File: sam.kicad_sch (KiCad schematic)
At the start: 46 parts, among them IC1 4164, IC10 74ACT138, IC15 MC6883, IC16 74LS244N, IC2 4164, IC3 4164, IC31 74LS02N, IC33 74ACT138N, IC36 74LS132, IC37 GAL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

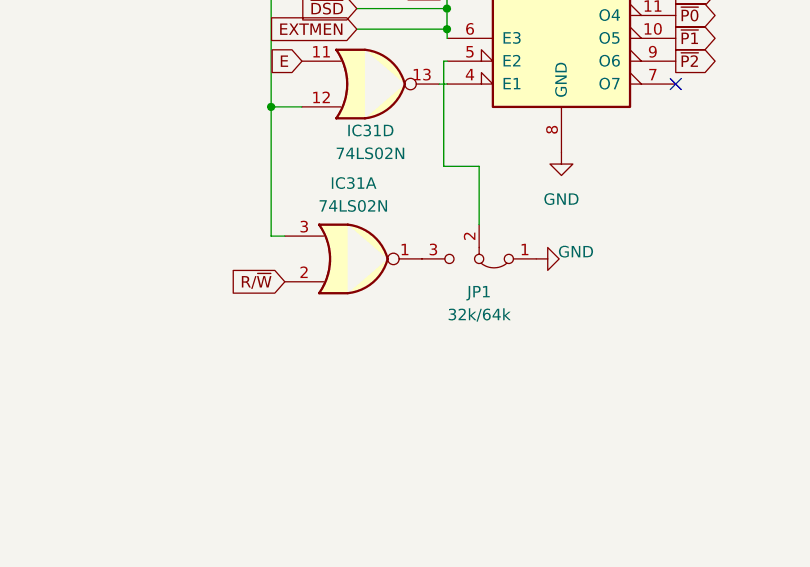
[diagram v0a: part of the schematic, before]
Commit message: rework keyboard type selection
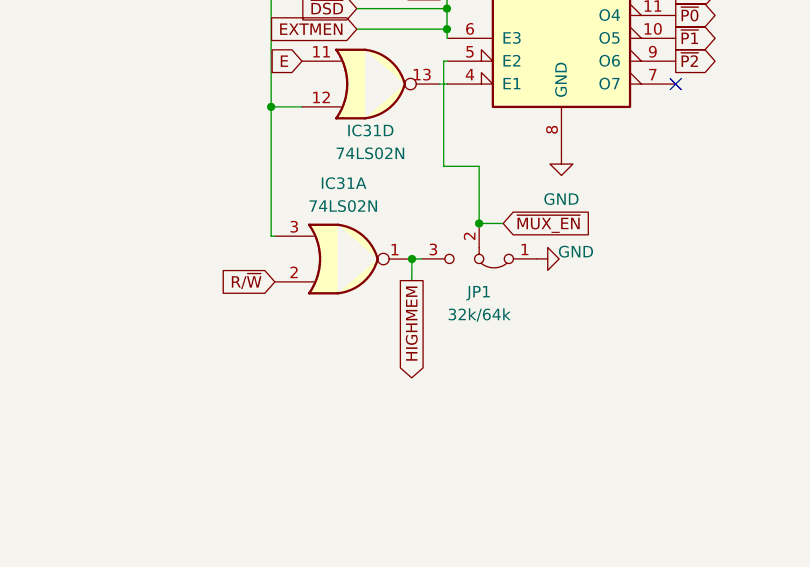
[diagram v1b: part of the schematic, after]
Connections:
- net ~{MUX_EN}: now reaches IC33.5 (E2), JP1.2 (C)
- net HIGHMEM: now reaches IC31.1, JP1.3 (B)
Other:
- moved on the sheet: IC31A
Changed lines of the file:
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@@
 	)
 	(junction
+		(at 112.903 191.77)
+		(diameter 0)
+		(color 0 0 0 0)
+	)
+	(junction
 		(at 89.789 163.576)
 		(diameter 0)
@@
 	)
 	(junction
+		(at 105.4417 195.7201)
+		(diameter 0)
+		(color 0 0 0 0)
+	)
+	(junction
 		(at 66.929 85.344)
 		(diameter 0)
@@
 	(wire
 		(pts
-			(xy 89.789 193.167) (xy 91.313 193.167)
+			(xy 89.789 193.167) (xy 90.2017 193.1801)
 		)
 		(stroke
@@
 	(wire
 		(pts
+			(xy 105.4417 195.7201) (xy 106.553 195.707)
+		)
+		(stroke
+			(width 0)
+			(type default)
+		)
+	)
+	(wire
+		(pts
 			(xy 244.856 24.003) (xy 244.856 24.384)
 		)
@@
 	(wire
 		(pts
-			(xy 112.903 185.42) (xy 112.903 191.897)
+			(xy 112.903 185.42) (xy 112.903 191.77)
 		)
 		(stroke
@@
 	(wire
 		(pts
+			(xy 115.57 191.77) (xy 112.903 191.77)
+		)
+		(stroke
+			(width 0)
+			(type default)
+		)
+	)
+	(wire
+		(pts
 			(xy 24.257 85.344) (xy 25.273 85.344)
 		)
@@
 	(wire
 		(pts
+			(xy 105.41 198.12) (xy 105.4417 195.7201)
+		)
+		(stroke
+			(width 0)
+			(type default)
+		)
+	)
+	(wire
+		(pts
 			(xy 221.742 75.311) (xy 232.156 75.311)
 		)
@@
 	(wire
 		(pts
+			(xy 112.903 191.77) (xy 112.903 191.897)
+		)
+		(stroke
+			(width 0)
+			(type default)
+		)
+	)
+	(wire
+		(pts
 			(xy 24.257 21.717) (xy 24.257 24.638)
 		)
@@
 	(global_label "R{slash}~{W}"
 		(shape input)
-		(at 91.313 198.247 180)
+		(at 90.2017 198.2601 180)
 		(fields_autoplaced yes)
 		(effects
@@
 		)
 		(property "Intersheetrefs" "${INTERSHEET_REFS}"
-			(at 85.0095 198.247 0)
+			(at 83.8982 198.2601 0)
 			(effects
 				(font
@@
 		)
 	)
+	(global_label "~{MUX_EN}"
+		(shape input)
+		(at 115.57 191.77 0)
+		(fields_autoplaced yes)
+		(effects
+			(font
+				(size 1.27 1.27)
+			)
+			(justify left)
+		)
+		(property "Intersheetrefs" "${INTERSHEET_REFS}"
+			(at 125.3395 191.77 0)
+			(effects
+				(font
+					(size 1.27 1.27)
+				)
+				(justify left)
+				(hide yes)
+			)
+		)
+	)
 	(global_label "~{DSD}"
 		(shape output)
@@
 		)
 	)
+	(global_label "HIGHMEM"
+		(shape output)
+		(at 105.41 198.12 270)
+		(fields_autoplaced yes)
+		(effects
+			(font
+				(size 1.27 1.27)
+			)
+			(justify right)
+		)
+		(property "Intersheetrefs" "${INTERSHEET_REFS}"
+			(at 105.41 209.0386 90)
+			(effects
+				(font
+					(size 1.27 1.27)
+				)
+				(justify right)
+				(hide yes)
+			)
+		)
+	)
 	(global_label "Z5"
 		(shape input)
@@
 	(symbol
 		(lib_id "74xx:74LS02")
-		(at 98.933 195.707 0)
+		(at 97.8217 195.7201 0)
 		(mirror x)
 		(unit 1)
@@
 		(fields_autoplaced yes)
 		(property "Reference" "IC31"
-			(at 98.933 187.325 0)
+			(at 97.8217 187.3381 0)
 			(effects
 				(font
@@
 		)
 		(property "Value" "74LS02N"
-			(at 98.933 189.865 0)
+			(at 97.8217 189.8781 0)
 			(effects
 				(font
@@
 		)
 		(property "Footprint" "Package_DIP:DIP-14_W7.62mm"
-			(at 98.933 195.707 0)
+			(at 97.8217 195.7201 0)
 			(effects
 				(font
@@
 		)
 		(property "Datasheet" "http://www.ti.com/lit/gpn/sn74ls02"
-			(at 98.933 195.707 0)
+			(at 97.8217 195.7201 0)
 			(effects
 				(font
@@
 		)
 		(property "Description" ""
-			(at 98.933 195.707 0)
+			(at 97.8217 195.7201 0)
 			(effects
 				(font
@@
 		)
 		(property "DigiKey" "296-1627-5-ND"
-			(at 98.933 195.707 0)
+			(at 97.8217 195.7201 0)
 			(effects
 				(font
@@
 		)
 		(property "SA2120" "Sheet 1 (spare)"
-			(at 98.933 195.707 0)
+			(at 97.8217 195.7201 0)
 			(effects
 				(font

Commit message: refresh BOM
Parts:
- C10, C12: value 100n -> 100nF; LCSC (none) -> C1711
- C40: LCSC (none) -> C1653
- C41: LCSC (none) -> C1663
- IC1, IC15, IC2, IC3, IC33, IC4, IC5, IC6, IC7, IC8: SA2120 Sheet 1 -> (none)
- IC10: LCSC (none) -> C1547282
- IC16: LCSC (none) -> C22374098; SA2120 Sheet 1 -> (none)
- IC31: LCSC (none) -> C22374091; SA2120 Sheet 1 (spare) -> (none)
- R12: DigiKey CF14JT22R0CT-ND -> (none); LCSC (none) -> C17561
- R19, R20, R21, R22, R23, R24, R25, R26, R27, R28, R66: LCSC (none) -> C17561
- R37: LCSC (none) -> C22843
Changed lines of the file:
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@@
 			)
 		)
-		(property "SA2120" "Sheet 1"
-			(at 35.433 42.418 0)
-			(effects
-				(font
-					(size 1.27 1.27)
-				)
-				(hide yes)
-			)
-		)
 		(pin "1"
 		)
@@
 			)
 		)
-		(property "Value" "100n"
+		(property "Value" "100nF"
 			(at 240.157 155.829 0)
 			(effects
@@
 			)
 		)
+		(property "LCSC" "C1711"
+			(at 237.236 154.686 0)
+			(effects
+				(font
+					(size 1.27 1.27)
+				)
+				(hide yes)
+			)
+		)
 		(pin "1"
 		)
@@
 			)
 		)
+		(property "LCSC" "C1547282"
+			(at 38.1 229.87 0)
+			(effects
+				(font
+					(size 1.27 1.27)
+				)
+				(hide yes)
+			)
+		)
 		(pin "1"
 		)
@@
 			)
 		)
-		(property "SA2120" "Sheet 1"
-			(at 120.777 42.545 0)
-			(effects
-				(font
-					(size 1.27 1.27)
-				)
-				(hide yes)
-			)
-		)
 		(pin "1"
 		)
@@
 			)
 		)
-		(property "SA2120" "Sheet 1"
+		(property "LCSC" "C22374098"
 			(at 35.306 168.91 0)
 			(effects
@@
 			)
 		)
+		(property "LCSC" "C17561"
+			(at 260.096 42.291 90)
+			(effects
+				(font
+					(size 1.27 1.27)
+				)
+				(hide yes)
+			)
+		)
 		(pin "1"
 		)
@@
 			)
 		)
+		(property "LCSC" "C17561"
+			(at 260.096 54.991 90)
+			(effects
+				(font
+					(size 1.27 1.27)
+				)
+				(hide yes)
+			)
+		)
 		(pin "1"
 		)
@@
 			)
 		)
+		(property "LCSC" "C17561"
+			(at 265.1564 169.6706 90)
+			(effects
+				(font
+					(size 1.27 1.27)
+				)
+				(hide yes)
+			)
+		)
 		(pin "1"
 		)
@@
 			)
 		)
-		(property "SA2120" "Sheet 1 (spare)"
+		(property "LCSC" "C22374091"
 			(at 100.838 176.276 0)
 			(effects
@@
 			)
 		)
-		(property "SA2120" "Sheet 1"
-			(at 122.047 166.116 0)
-			(effects
-				(font
-					(size 1.27 1.27)
-				)
-				(hide yes)
-			)
-		)
 		(pin "1"
 		)
@@
 			)
 		)
-		(property "SA2120" "Sheet 1"
-			(at 78.105 42.418 0)
-			(effects
-				(font
-					(size 1.27 1.27)
-				)
-				(hide yes)
-			)
-		)
 		(pin "1"
 		)
@@
 			)
 		)
+		(property "LCSC" "C22843"
+			(at 225.298 88.011 90)
+			(effects
+				(font
+					(size 1.27 1.27)
+				)
+				(hide yes)
+			)
+		)
 		(pin "1"
 		)
@@
 			)
 		)
+		(property "LCSC" "C1663"
+			(at 218.186 88.011 90)
+			(effects
+				(font
+					(size 1.27 1.27)
+				)
+				(hide yes)
+			)
+		)
 		(pin "1"
 		)
@@
 			)
 		)
+		(property "LCSC" "C1653"
+			(at 218.186 75.311 90)
+			(effects
+				(font
+					(size 1.27 1.27)
+				)
+				(hide yes)
+			)
+		)
 		(pin "1"
 		)
@@
 			)
 		)
-		(property "Value" "100n"
+		(property "Value" "100nF"
 			(at 373.253 199.263 0)
 			(effects
@@
 			)
 		)
+		(property "LCSC" "C1711"
+			(at 370.332 198.12 0)
+			(effects
+				(font
+					(size 1.27 1.27)
+				)
+				(hide yes)
+			)
+		)
 		(pin "1"
 		)
@@
 			)
 		)
-		(property "SA2120" "Sheet 1 (spare)"
+		(property "LCSC" "C22374091"
 			(at 97.8217 195.7201 0)
 			(effects
@@
 			)
 		)
-		(property "SA2120" "Sheet 1"
-			(at 120.777 103.251 0)
-			(effects
-				(font
-					(size 1.27 1.27)
-				)
-				(hide yes)
-			)
-		)
 		(pin "1"
 		)
@@
 			)
 		)
+		(property "LCSC" "C17561"
+			(at 260.096 34.671 90)
+			(effects
+				(font
+					(size 1.27 1.27)
+				)
+				(hide yes)
+			)
+		)
 		(pin "1"
 		)
@@
 			)
 		)
+		(property "LCSC" "C17561"
+			(at 279.0264 52.4585 90)
+			(effects
+				(font
+					(size 1.27 1.27)
+				)
+				(hide yes)
+			)
+		)
 		(pin "1"
 		)
@@
 			)
 		)
+		(property "LCSC" "C17561"
+			(at 260.096 29.591 90)
+			(effects
+				(font
+					(size 1.27 1.27)
+				)
+				(hide yes)
+			)
+		)
 		(pin "1"
 		)
@@
 			)
 		)
-		(property "SA2120" "Sheet 1"
-			(at 35.433 103.124 0)
-			(effects
-				(font
-					(size 1.27 1.27)
-				)
-				(hide yes)
-			)
-		)
 		(pin "1"
 		)
@@
 			)
 		)
-		(property "SA2120" "Sheet 1"
-			(at 163.449 103.251 0)
-			(effects
-				(font
-					(size 1.27 1.27)
-				)
-				(hide yes)
-			)
-		)
 		(pin "1"
 		)
@@
 			)
 		)
-		(property "SA2120" "Sheet 1"
-			(at 163.449 42.545 0)
-			(effects
-				(font
-					(size 1.27 1.27)
-				)
-				(hide yes)
-			)
-		)
 		(pin "1"
 		)
@@
 			)
 		)
-		(property "DigiKey" "CF14JT22R0CT-ND"
+		(property "DigiKey" ""
 			(at 260.096 49.911 0)
 			(effects
@@
 			)
 		)
+		(property "LCSC" "C17561"
+			(at 260.096 49.911 90)
+			(effects
+				(font
+					(size 1.27 1.27)
+				)
+				(hide yes)
+			)
+		)
 		(pin "1"
 		)
@@
 			)
 		)
+		(property "LCSC" "C17561"
+			(at 260.096 37.211 90)
+			(effects
+				(font
+					(size 1.27 1.27)
+				)
+				(hide yes)
+			)
+		)
 		(pin "1"
 		)
@@
 			)
 		)
+		(property "LCSC" "C17561"
+			(at 260.096 44.831 90)
+			(effects
+				(font
+					(size 1.27 1.27)
+				)
+				(hide yes)
+			)
+		)
 		(pin "1"
 		)
@@
 			)
 		)
-		(property "SA2120" "Sheet 1"
-			(at 78.105 103.124 0)
-			(effects
-				(font
-					(size 1.27 1.27)
-				)
-				(hide yes)
-			)
-		)
 		(pin "1"
 		)
@@
 			)
 		)
+		(property "LCSC" "C17561"
+			(at 260.096 32.131 90)
+			(effects
+				(font
+					(size 1.27 1.27)
+				)
+				(hide yes)
+			)
+		)
 		(pin "1"
 		)
@@
 			)
 		)
+		(property "LCSC" "C17561"
+			(at 260.096 39.751 90)
+			(effects
+				(font
+					(size 1.27 1.27)
+				)
+				(hide yes)
+			)
+		)
 		(pin "1"
 		)
@@
 			)
 		)
-		(property "SA2120" "Sheet 1"
-			(at 244.856 60.071 0)
-			(effects
-				(font
-					(size 1.27 1.27)
-				)
-				(hide yes)
-			)
-		)
 		(pin "1"
 		)
@@
 			(effects
 				(font
+					(size 1.27 1.27)
+				)
+				(hide yes)
+			)
+		)
+		(property "LCSC" "C17561"
+			(at 260.096 57.531 90)
+			(effects
+				(font
